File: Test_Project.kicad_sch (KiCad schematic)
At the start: 4 parts, among them U1 STM32L081KZTx, U2 MIC2132YML

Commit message: Daily commit
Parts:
- added R1: 10k, Resistor_SMD:R_0805_2012Metric_Pad1.20x1.40mm_HandSolder, symbol Device:R_Small
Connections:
- net GNDREF: now also R1.2
- net SWDIO: now reaches U1.23 (PA13)
- net SWCLK: now reaches U1.24 (PA14)
- net at U1.31 (BOOT0): now also R1.1
- net LED_Data_Out (PWM): now reaches U1.8 (PA2)
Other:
- moved on the sheet: C1
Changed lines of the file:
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@@
 	(wire
 		(pts
-			(xy 34.29 132.08) (xy 67.31 132.08)
+			(xy 115.57 167.64) (xy 97.79 167.64)
+		)
+		(stroke
+			(width 0)
+			(type default)
+		)
+	)
+	(wire
+		(pts
+			(xy 115.57 165.1) (xy 97.79 165.1)
+		)
+		(stroke
+			(width 0)
+			(type default)
+		)
+	)
+	(wire
+		(pts
+			(xy 31.75 132.08) (xy 67.31 132.08)
 		)
 		(stroke
@@
 	(wire
 		(pts
+			(xy 97.79 137.16) (xy 121.92 137.16)
+		)
+		(stroke
+			(width 0)
+			(type default)
+		)
+	)
+	(wire
+		(pts
+			(xy 45.72 137.16) (xy 67.31 137.16)
+		)
+		(stroke
+			(width 0)
+			(type default)
+		)
+	)
+	(wire
+		(pts
 			(xy 50.8 57.15) (xy 63.5 57.15)
 		)
@@
 	(wire
 		(pts
-			(xy 34.29 133.35) (xy 34.29 132.08)
-		)
-		(stroke
-			(width 0)
-			(type default)
+			(xy 31.75 137.16) (xy 31.75 132.08)
+		)
+		(stroke
+			(width 0)
+			(type default)
+		)
+	)
+	(label "LED_Data_Out (PWM)"
+		(at 101.6 137.16 0)
+		(effects
+			(font
+				(size 1.27 1.27)
+			)
+			(justify left bottom)
+		)
+	)
+	(label "SWDIO"
+		(at 109.22 165.1 0)
+		(effects
+			(font
+				(size 1.27 1.27)
+			)
+			(justify left bottom)
+		)
+	)
+	(label "SWCLK"
+		(at 109.22 167.64 0)
+		(effects
+			(font
+				(size 1.27 1.27)
+			)
+			(justify left bottom)
 		)
 	)
 	(symbol
 		(lib_id "power:GNDREF")
-		(at 34.29 138.43 0)
+		(at 45.72 142.24 0)
+		(unit 1)
+		(exclude_from_sim no)
+		(in_bom yes)
+		(on_board yes)
+		(dnp no)
+		(fields_autoplaced yes)
+		(property "Reference" "#PWR02"
+			(at 45.72 148.59 0)
+			(effects
+				(font
+					(size 1.27 1.27)
+				)
+				(hide yes)
+			)
+		)
+		(property "Value" "GNDREF"
+			(at 45.72 147.32 0)
+			(effects
+				(font
+					(size 1.27 1.27)
+				)
+			)
+		)
+		(property "Footprint" ""
+			(at 45.72 142.24 0)
+			(effects
+				(font
+					(size 1.27 1.27)
+				)
+				(hide yes)
+			)
+		)
+		(property "Datasheet" ""
+			(at 45.72 142.24 0)
+			(effects
+				(font
+					(size 1.27 1.27)
+				)
+				(hide yes)
+			)
+		)
+		(property "Description" "Power symbol creates a global label with name \"GNDREF\" , reference supply ground"
+			(at 45.72 142.24 0)
+			(effects
+				(font
+					(size 1.27 1.27)
+				)
+				(hide yes)
+			)
+		)
+		(pin "1"
+		)
+		(instances
+			(project "Test_Project"
+				(path "/1d634910-d974-4dae-8aa3-77282bd573f9"
+					(reference "#PWR02")
+					(unit 1)
+				)
+			)
+		)
+	)
+	(symbol
+		(lib_id "power:GNDREF")
+		(at 31.75 142.24 0)
 		(unit 1)
 		(exclude_from_sim no)
@@
 		(fields_autoplaced yes)
 		(property "Reference" "#PWR01"
-			(at 34.29 144.78 0)
+			(at 31.75 148.59 0)
 			(effects
 				(font
@@
 		)
 		(property "Value" "GNDREF"
-			(at 34.29 143.51 0)
+			(at 31.75 147.32 0)
 			(effects
 				(font
@@
 		)
 		(property "Footprint" ""
-			(at 34.29 138.43 0)
+			(at 31.75 142.24 0)
 			(effects
 				(font
@@
 		)
 		(property "Datasheet" ""
-			(at 34.29 138.43 0)
+			(at 31.75 142.24 0)
 			(effects
 				(font
@@
 		)
 		(property "Description" "Power symbol creates a global label with name \"GNDREF\" , reference supply ground"
-			(at 34.29 138.43 0)
+			(at 31.75 142.24 0)
 			(effects
 				(font
@@
 				(path "/1d634910-d974-4dae-8aa3-77282bd573f9"
 					(reference "#PWR01")
+					(unit 1)
+				)
+			)
+		)
+	)
+	(symbol
+		(lib_id "Device:R_Small")
+		(at 45.72 139.7 0)
+		(unit 1)
+		(exclude_from_sim no)
+		(in_bom yes)
+		(on_board yes)
+		(dnp no)
+		(fields_autoplaced yes)
+		(property "Reference" "R1"
+			(at 48.26 138.4299 0)
+			(effects
+				(font
+					(size 1.016 1.016)
+				)
+				(justify left)
+			)
+		)
+		(property "Value" "10k"
+			(at 48.26 140.9699 0)
+			(effects
+				(font
+					(size 1.27 1.27)
+				)
+				(justify left)
+			)
+		)
+		(property "Footprint" "Resistor_SMD:R_0805_2012Metric_Pad1.20x1.40mm_HandSolder"
+			(at 45.72 139.7 0)
+			(effects
+				(font
+					(size 1.27 1.27)
+				)
+				(hide yes)
+			)
+		)
+		(property "Datasheet" "~"
+			(at 45.72 139.7 0)
+			(effects
+				(font
+					(size 1.27 1.27)
+				)
+				(hide yes)
+			)
+		)
+		(property "Description" "Resistor, small symbol"
+			(at 45.72 139.7 0)
+			(effects
+				(font
+					(size 1.27 1.27)
+				)
+				(hide yes)
+			)
+		)
+		(pin "2"
+		)
+		(pin "1"
+		)
+		(instances
+			(project ""
+				(path "/1d634910-d974-4dae-8aa3-77282bd573f9"
+					(reference "R1")
 					(unit 1)
 				)
@@
 	(symbol
 		(lib_id "Device:C_Small_US")
-		(at 34.29 135.89 0)
+		(at 31.75 139.7 0)
 		(unit 1)
 		(exclude_from_sim no)
@@
 		(fields_autoplaced yes)
 		(property "Reference" "C1"
-			(at 36.83 134.7469 0)
+			(at 34.29 138.5569 0)
 			(effects
 				(font
@@
 		)
 		(property "Value" "100nF"
-			(at 36.83 137.2869 0)
+			(at 34.29 141.0969 0)
 			(effects
 				(font
@@
 		)
 		(property "Footprint" "Capacitor_SMD:C_0603_1608Metric_Pad1.08x0.95mm_HandSolder"
-			(at 34.29 135.89 0)
+			(at 31.75 139.7 0)
 			(effects
 				(font
@@
 		)
 		(property "Datasheet" ""
-			(at 34.29 135.89 0)
+			(at 31.75 139.7 0)
 			(effects
 				(font
@@
 		)
 		(property "Description" "capacitor, small US symbol"
-			(at 34.29 135.89 0)
-			(effects
-				(font
+			(at 31.75 139.7 0)
+			(effects
+				(font

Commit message: Added a local symbol library to match how the PCB footprints are stored. Again, with portability in mind.
This update of footprints and schematic symbols should be done whenever something else is added.
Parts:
- C1: symbol Device:C_Small_US -> Library:C_Small_US
- J1: symbol Connector:Barrel_Jack_Switch_Pin3Ring -> Library:Barrel_Jack_Switch_Pin3Ring
- R1: symbol Device:R_Small -> Library:R_Small
- U1: symbol MCU_ST_STM32L0:STM32L081KZTx -> Library:STM32L081KZTx
- U2: symbol Custom_Lib:MIC2132YML -> Library:MIC2132YML
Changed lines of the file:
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@@
 	)
 	(symbol
-		(lib_id "Device:R_Small")
+		(lib_id "Library:R_Small")
 		(at 45.72 139.7 0)
 		(unit 1)
@@
 	)
 	(symbol
-		(lib_id "Connector:Barrel_Jack_Switch_Pin3Ring")
+		(lib_id "Library:Barrel_Jack_Switch_Pin3Ring")
 		(at 43.18 54.61 0)
 		(unit 1)
@@
 	)
 	(symbol
-		(lib_id "MCU_ST_STM32L0:STM32L081KZTx")
+		(lib_id "Library:STM32L081KZTx")
 		(at 82.55 152.4 0)
 		(unit 1)
@@
 	)
 	(symbol
-		(lib_id "Custom_Lib:MIC2132YML")
+		(lib_id "Library:MIC2132YML")
 		(at 123.19 74.93 0)
 		(unit 1)
@@
 	)
 	(symbol
-		(lib_id "Device:C_Small_US")
+		(lib_id "Library:C_Small_US")
 		(at 31.75 139.7 0)
 		(unit 1)

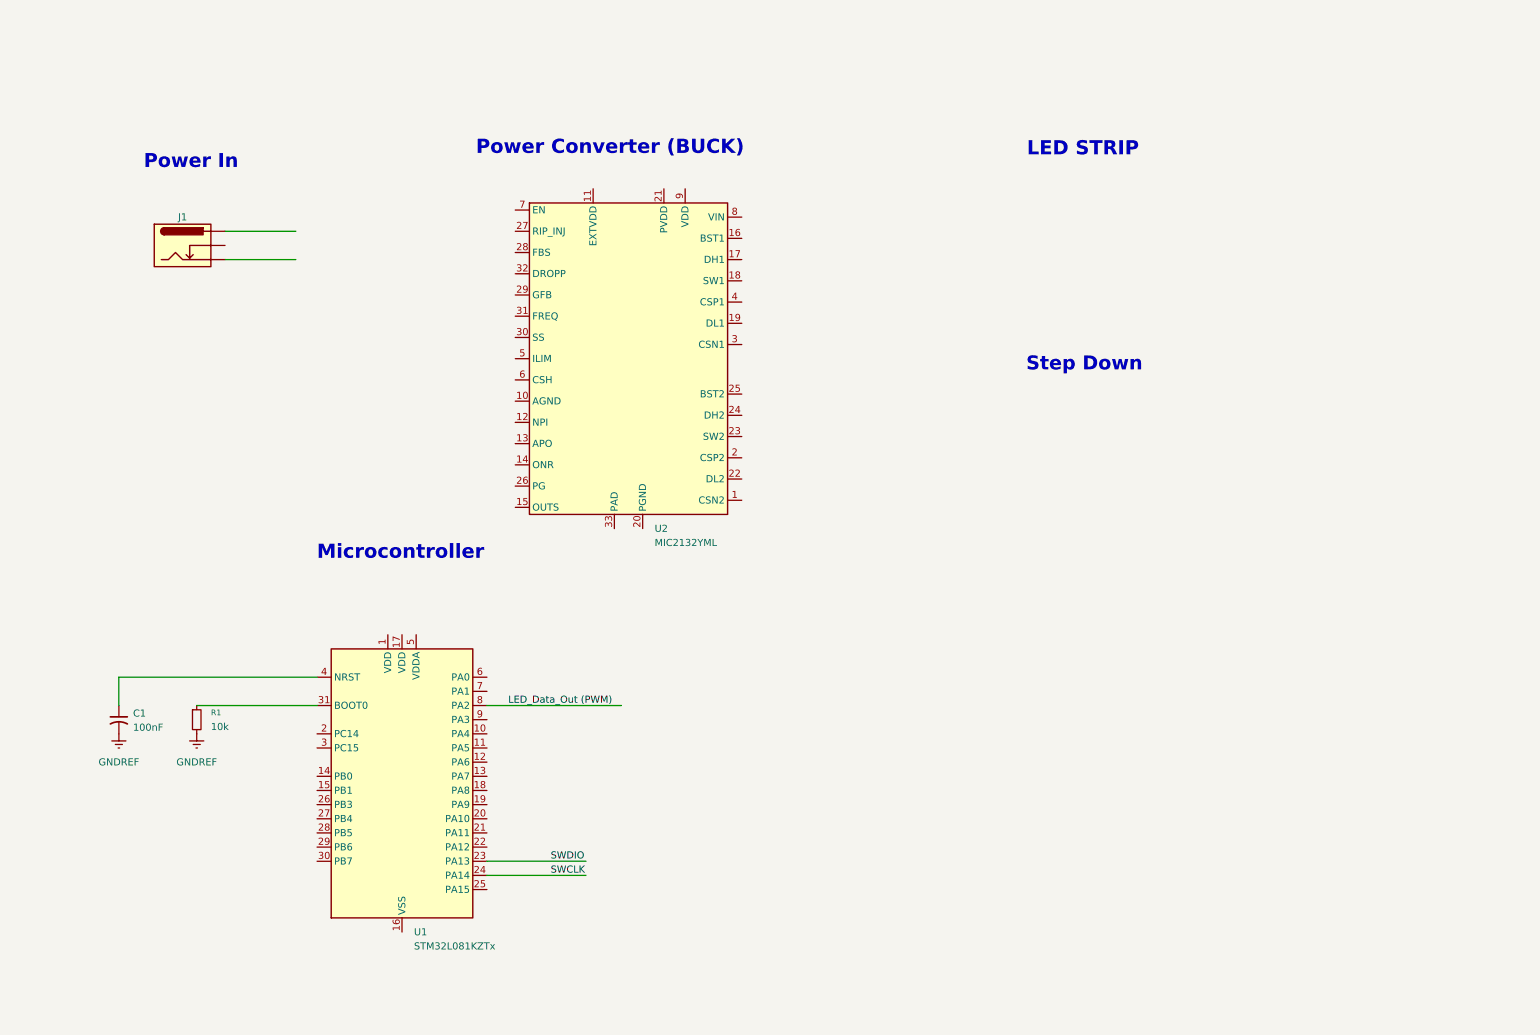
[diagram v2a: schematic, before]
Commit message: Worked on switching converter portion of schematic. Still needs deciding: 	RDROOP 	Cout 	RIlim 	Cin 	Bootstrap caps 	MOSFETs
MOSFET based level shifter for the LED strip.
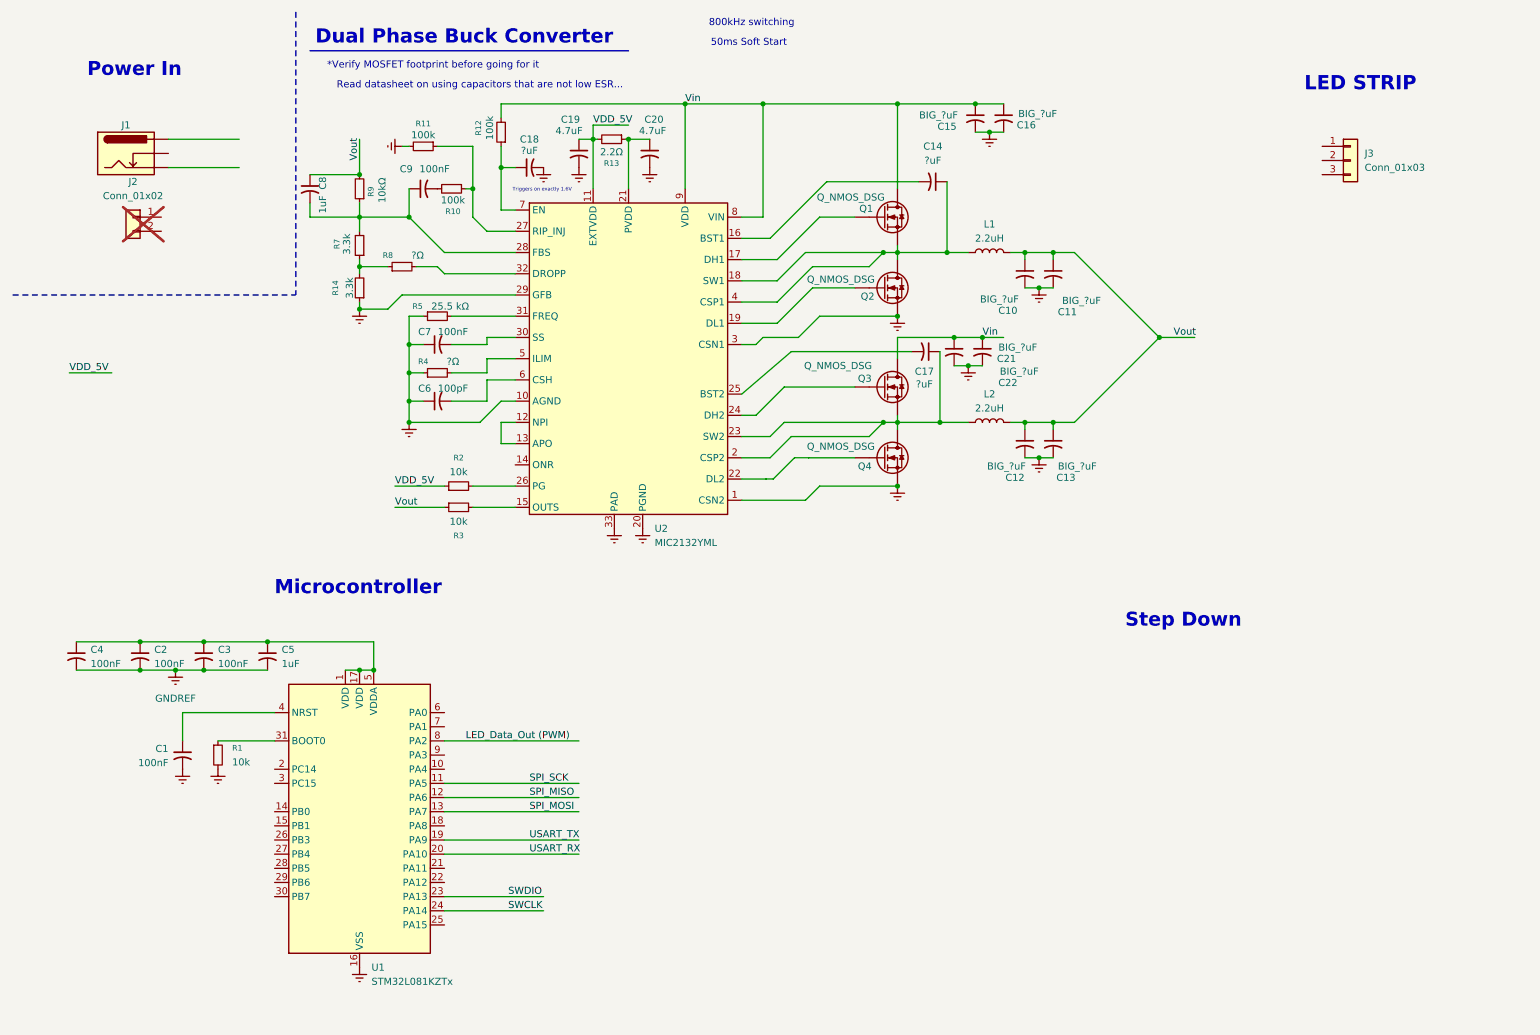
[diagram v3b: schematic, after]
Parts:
- added C10, C11, C12, C13, C15, C16, C21, C22: BIG_?uF, Capacitor_SMD:C_0805_2012Metric_Pad1.18x1.45mm_HandSolder, symbol Library:C_Small_US
- added C14, C17, C18: ?uF, Capacitor_SMD:C_0603_1608Metric_Pad1.08x0.95mm_HandSolder, symbol Library:C_Small_US
- added C19, C20: 4.7uF, Capacitor_SMD:C_0603_1608Metric_Pad1.08x0.95mm_HandSolder, symbol Library:C_Small_US
- added C2, C3, C4, C7, C9: 100nF, Capacitor_SMD:C_0603_1608Metric_Pad1.08x0.95mm_HandSolder, symbol Library:C_Small_US
- added C5, C8: 1uF, Capacitor_SMD:C_0603_1608Metric_Pad1.08x0.95mm_HandSolder, symbol Library:C_Small_US
- added C6: 100pF, Capacitor_SMD:C_0603_1608Metric_Pad1.08x0.95mm_HandSolder, symbol Library:C_Small_US
- added J2: Conn_01x02, Connector_PinHeader_2.54mm:PinHeader_1x02_P2.54mm_Vertical, symbol Connector_Generic:Conn_01x02
- added J3: Conn_01x03, Connector_PinHeader_2.54mm:PinHeader_1x03_P2.54mm_Vertical, symbol Connector_Generic:Conn_01x03
- added L1, L2: 2.2uH, symbol Device:L
- added Q1, Q2, Q3, Q4: Q_NMOS_DSG, symbol Transistor_FET:Q_NMOS_DSG
- added R10, R11, R12: 100k, Resistor_SMD:R_0805_2012Metric_Pad1.20x1.40mm_HandSolder, symbol Library:R_Small
- added R13: 2.2Ω, Resistor_SMD:R_0805_2012Metric_Pad1.20x1.40mm_HandSolder, symbol Library:R_Small
- added R14, R7: 3.3k, Resistor_SMD:R_0805_2012Metric_Pad1.20x1.40mm_HandSolder, symbol Library:R_Small
- added R2, R3: 10k, Resistor_SMD:R_0805_2012Metric_Pad1.20x1.40mm_HandSolder, symbol Library:R_Small
- added R4, R8: ?Ω, Resistor_SMD:R_0805_2012Metric_Pad1.20x1.40mm_HandSolder, symbol Library:R_Small
- added R5: 25.5 kΩ, Resistor_SMD:R_0805_2012Metric_Pad1.20x1.40mm_HandSolder, symbol Library:R_Small
- added R9: 10kΩ, Resistor_SMD:R_0805_2012Metric_Pad1.20x1.40mm_HandSolder, symbol Library:R_Small
- J1: now left out of the parts list
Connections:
- net GNDREF: now also C2.2, C3.2, C4.2, C5.2; no longer C1.2, R1.2
- net at U1.1 (VDD): now also U1.17 (VDD), U1.5 (VDDA), C2.1, C3.1, C4.1, C5.1
- net SPI_SCK: now reaches U1.11 (PA5)
- net SPI_MISO: now reaches U1.12 (PA6)
- net SPI_MOSI: now reaches U1.13 (PA7)
- net USART_TX: now reaches U1.19 (PA9)
- net USART_RX: now reaches U1.20 (PA10)
- net at U2.1 (CSN2): now also Q4.2 (S)
- net at U2.10 (AGND): now also C6.1, C7.1, R4.1, R5.1
- net VDD_5V: now reaches U2.11 (EXTVDD)
- net VDD_5V: now also C19.1, R13.2, R2.1
- net at U2.12 (NPI): now also U2.13 (APO)
- net at U2.15 (OUTS): now also R3.2
- net at U2.16 (BST1): now also C14.2
- net at U2.17 (DH1): now also Q1.3 (G)
- net at U2.18 (SW1): now also U2.4 (CSP1), C14.1, L1.1, Q1.2 (S), Q2.1 (D)
- net at U2.19 (DL1): now also Q2.3 (G)
- net at U2.2 (CSP2): now also U2.23 (SW2), C17.1, L2.1, Q3.2 (S), Q4.1 (D)
- net at U2.21 (PVDD): now also C20.1, R13.1
- net at U2.22 (DL2): now also Q4.3 (G)
- net at U2.24 (DH2): now also Q3.3 (G)
- net at U2.25 (BST2): now also C17.2
- net at U2.26 (PG): now also R2.2
- net at U2.27 (RIP_INJ): now also R10.1, R11.1
- net at U2.28 (FBS): now also C8.2, C9.1, R7.2, R9.1
- net at U2.29 (GFB): now also R14.1
- net at U2.3 (CSN1): now also Q2.2 (S)
- net at U2.30 (SS): now also C7.2
- net at U2.31 (FREQ): now also R5.2
- net at U2.32 (DROPP): now also R8.2
- net at U2.5 (ILIM): now also R4.2
- net at U2.6 (CSH): now also C6.2
- net at U2.7 (EN): now also C18.1, R12.1
- net Vin: now reaches U2.8 (VIN)
- net Vin: now also U2.9 (VDD), C15.1, C16.1, C21.1, C22.1, Q1.1 (D), Q3.1 (D), R12.2
- new net: C21.2, C22.2
- new net: C15.2, C16.2
- new net: C12.2, C13.2
- new net: R14.2, R7.1, R8.1
- new net: C9.2, R10.2
- new net: C10.2, C11.2
- new net Vout: C10.1, C11.1, C12.1, C13.1, C8.1, L1.2, L2.2, R3.1, R9.2
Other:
- note added: "*Verify MOSFET footprint before going for it"
- note added: "50ms Soft Start"
- note added: "800kHz switching"
- note added: "Dual Phase Buck Converter"
- note added: "Read datasheet on using capacitors that are not low ESR..."
- note added: "Triggers on exactly 1.6V"
- note removed: "Power Converter (BUCK)"
- moved on the sheet: C1, J1, R1, U1

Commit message: Finished up buck section of schematic minus the mosfet choice. Also moved around things on the schematic and added an optional electrolytic capacitor
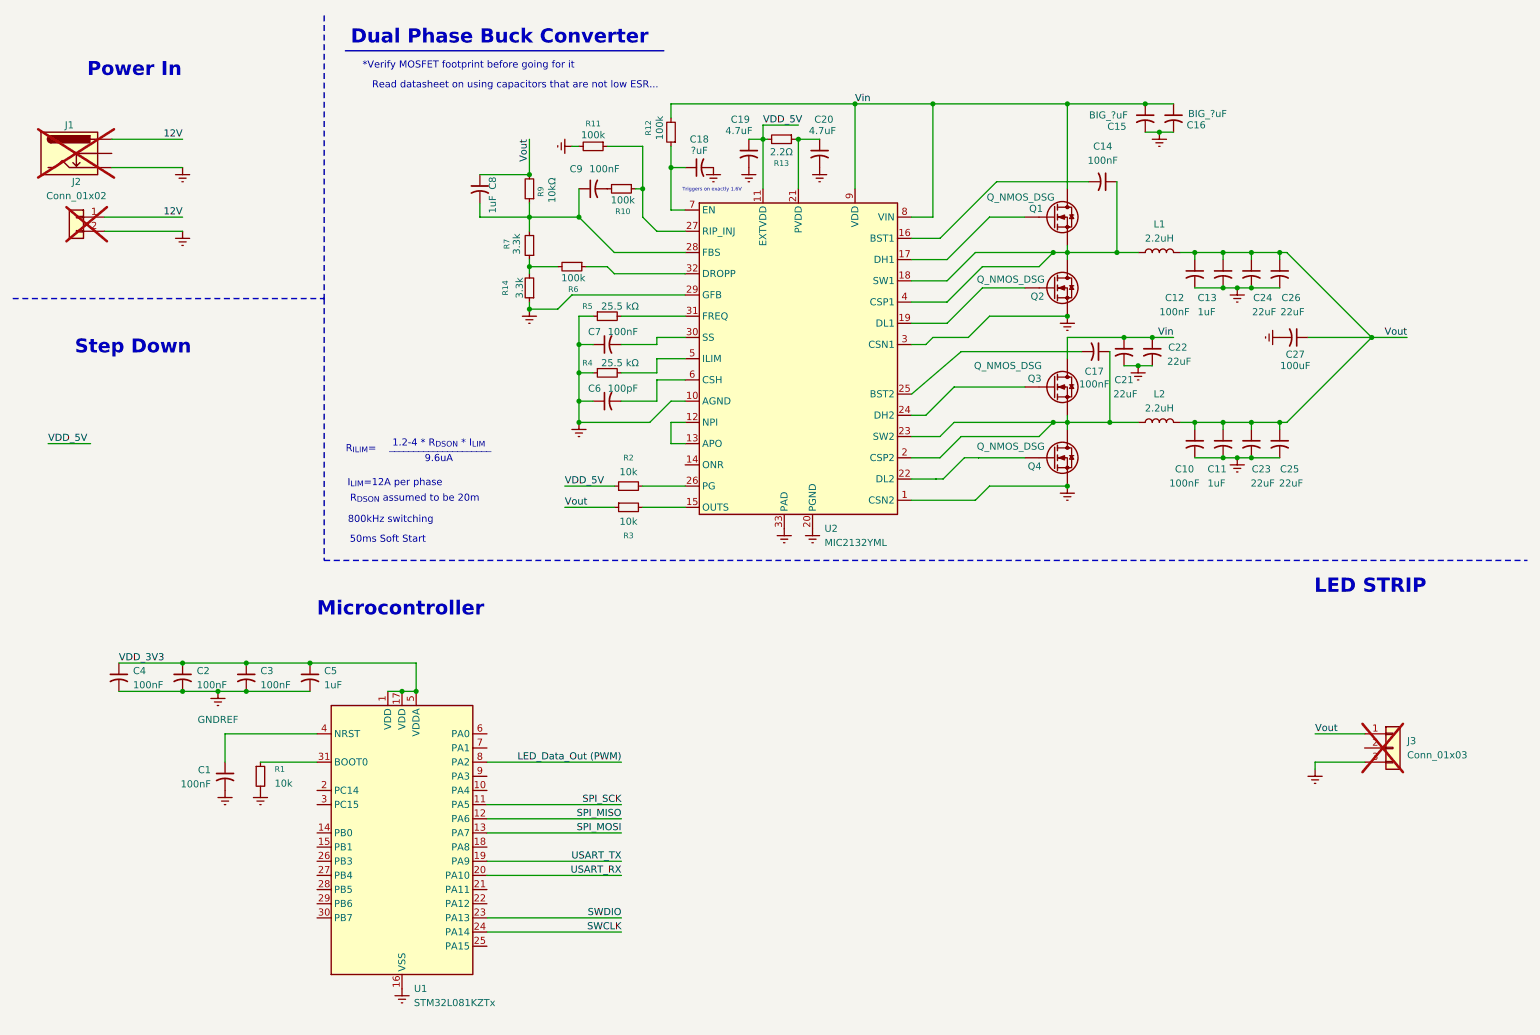
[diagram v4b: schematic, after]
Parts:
- removed R8: ?Ω, Resistor_SMD:R_0805_2012Metric_Pad1.20x1.40mm_HandSolder, symbol Library:R_Small
- added C23, C24, C25, C26: 22uF, Capacitor_SMD:C_0805_2012Metric_Pad1.18x1.45mm_HandSolder, symbol Library:C_Small_US
- added C27: 100uF, Capacitor_THT:CP_Radial_D6.3mm_P2.50mm, symbol Library:C_Small_US
- added R6: 100k, Resistor_SMD:R_0805_2012Metric_Pad1.20x1.40mm_HandSolder, symbol Library:R_Small
- C10, C12: value BIG_?uF -> 100nF; footprint Capacitor_SMD:C_0805_2012Metric_Pad1.18x1.45mm_HandSolder -> Capacitor_SMD:C_0603_1608Metric_Pad1.08x0.95mm_HandSolder
- C11, C13: value BIG_?uF -> 1uF; footprint Capacitor_SMD:C_0805_2012Metric_Pad1.18x1.45mm_HandSolder -> Capacitor_SMD:C_0603_1608Metric_Pad1.08x0.95mm_HandSolder
- C14, C17: value ?uF -> 100nF
- C21, C22: value BIG_?uF -> 22uF
- J1: now not fitted
- J3: now not fitted; now left out of the parts list
- R4: value ?Ω -> 25.5 kΩ
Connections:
- net Vout: now also J3.1 (Pin_1), C23.1, C24.1, C25.1, C26.1, C27.1
- net VDD_3V3: now reaches C2.1, C3.1, C4.1, C5.1, U1.1 (VDD), U1.17 (VDD), U1.5 (VDDA)
- net 12V: now reaches J2.1 (Pin_1)
- net 12V: now also J1.1
- net at C12.2, C13.2: now also C24.2, C26.2
- net at R14.2, R7.1: now also R6.2
- net at U2.32 (DROPP): now also R6.1
- net at C10.2, C11.2: now also C23.2, C25.2
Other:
- note added: "1.2-4 * R_{DSON} * I_{LIM}"
- note added: "9.6uA"
- note added: "I_{LIM}=12A per phase"
- note added: "R_{DSON} assumed to be 20m"
- note added: "R_{ILIM}="
- note added: "_____________________"
- moved on the sheet: C1, C14, C15, C16, C17, C18, C19, C2, C20, C3, C4, C5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
